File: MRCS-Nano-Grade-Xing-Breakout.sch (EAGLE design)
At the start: 24 parts, among them M2 SMALL_SERVO

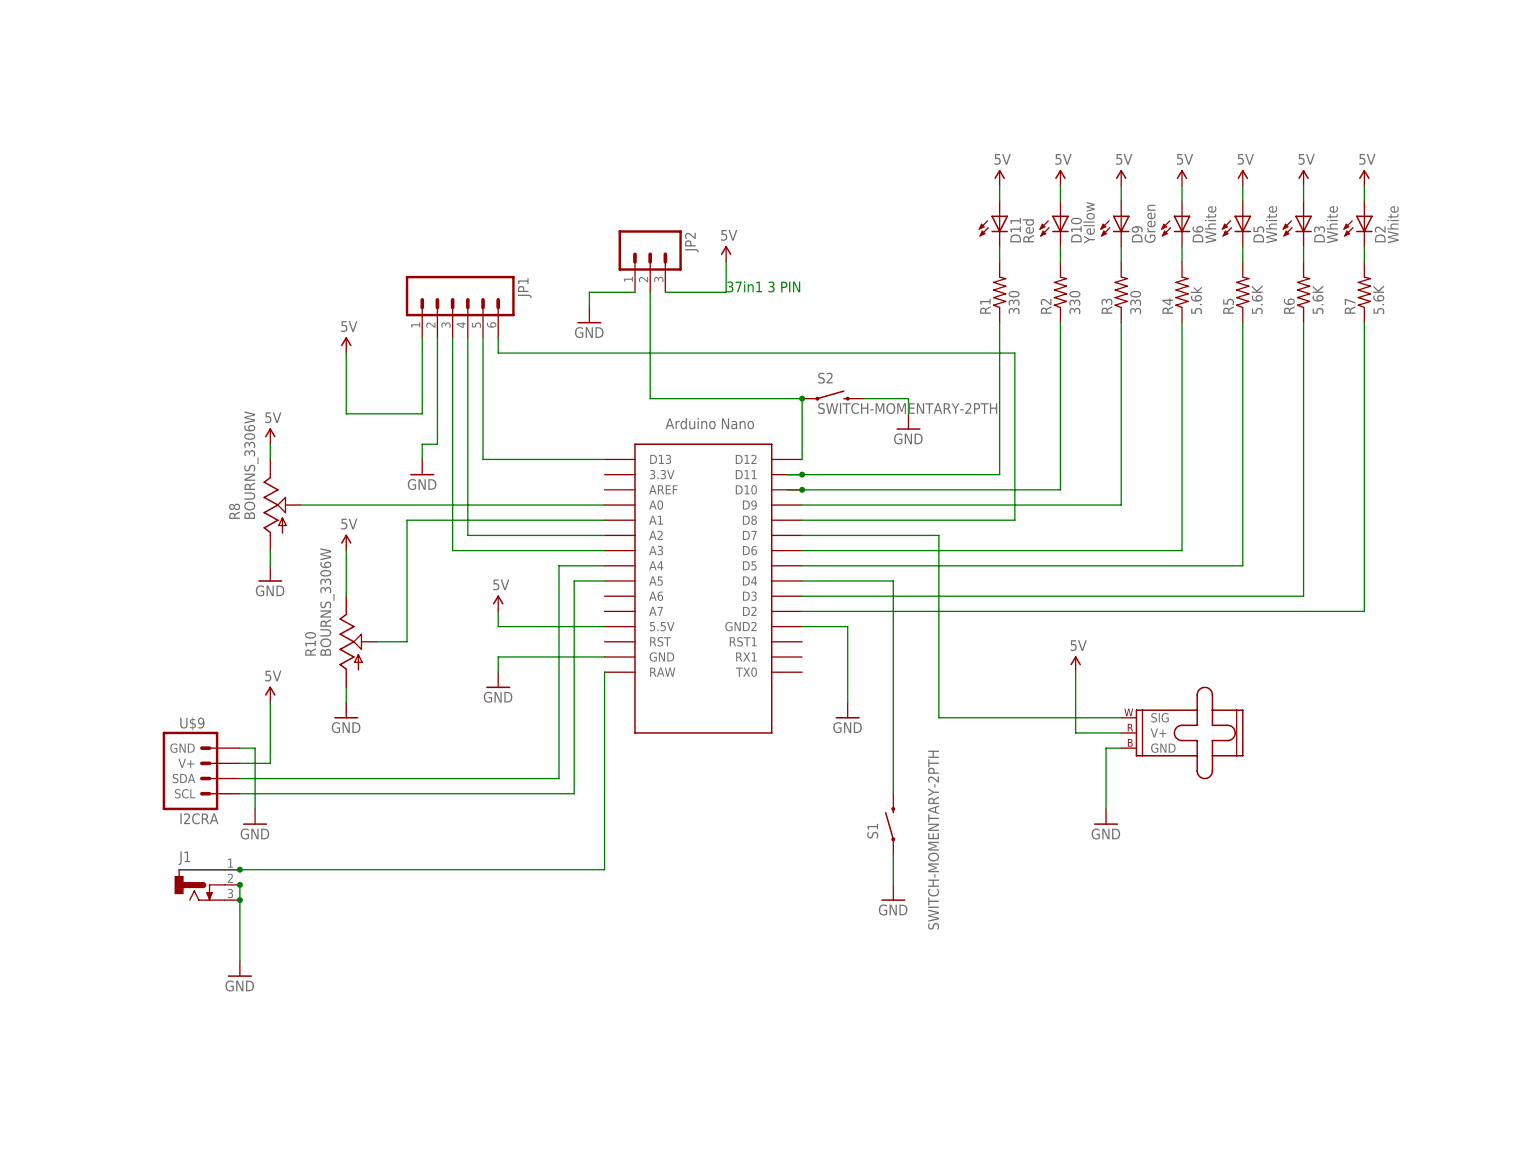
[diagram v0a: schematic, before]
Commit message: completed initial deisgn
After some consultation with Jon Schmidt this is ready to try for fab
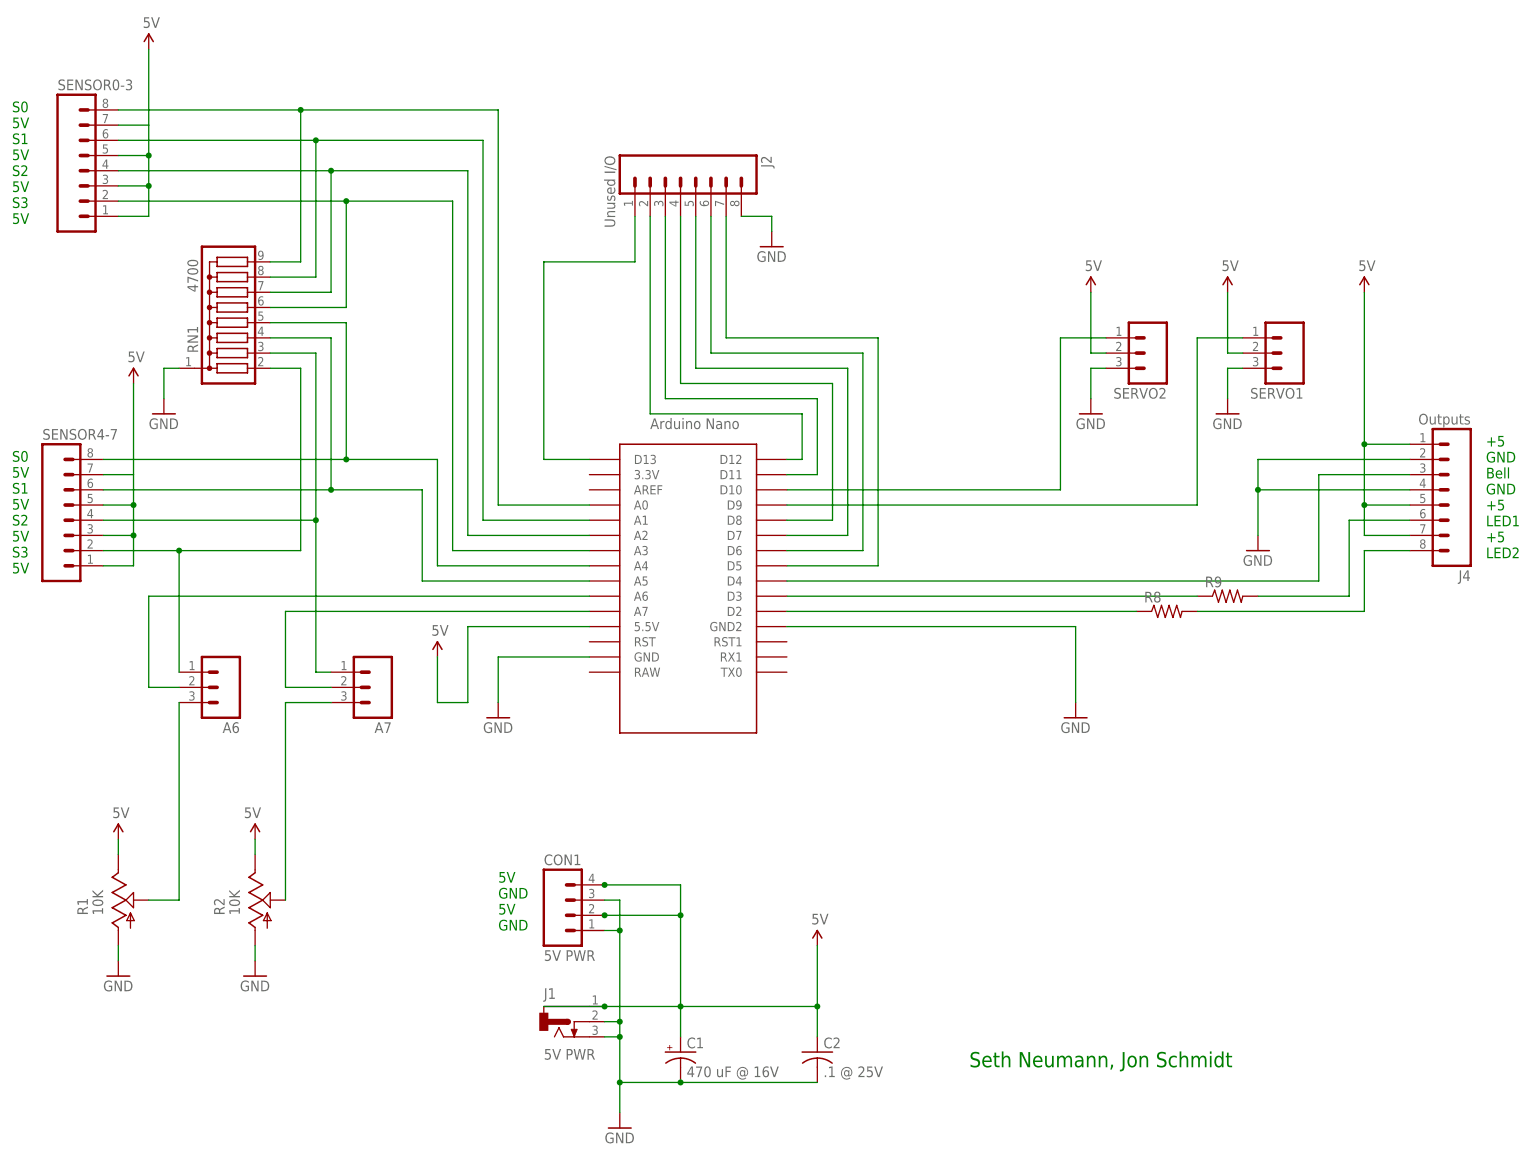
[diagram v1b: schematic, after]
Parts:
- removed D10: Yellow, SPCoast:LEDLED3MM
- removed D11: Red, SPCoast:LEDLED3MM
- removed D2, D3, D5, D6: White, SPCoast:LEDLED3MM
- removed D9: Green, SPCoast:LEDLED3MM
- removed JP1: (no value), SparkFun-Connectors:M06LOCK
- removed JP2: (no value), SparkFun-Connectors:M03LOCK
- removed M2: SMALL_SERVO, SparkFun-Electromechanical:SMALL_SERVO
- removed R10: BOURNS_3306W, mschutzer:BOURNS_3306W
- removed R3: 330, SparkFun-Resistors:RESISTORPTH-1/4W
- removed R4: 5.6k, SparkFun-Resistors:RESISTORPTH-1/4W
- removed R5, R6, R7: 5.6K, SparkFun-Resistors:RESISTORPTH-1/4W
- removed S1, S2: SWITCH-MOMENTARY-2PTH, SparkFun-Electromechanical:SWITCH-MOMENTARY-2PTH
- removed U$9: I2CRA, SPCoast-minimal:I2CRA
- added A6, A7, SERVO1, SERVO2: (no value), SparkFun-Connectors:M03LOCK
- added C1: 470 uF @ 16V, SPCoast:CAP-POLPTH-3.5MM
- added C2: .1 @ 25V, SPCoast:CAPPTH2
- added CON1: 5V PWR, SPCoast:CONNECTOR-M04SCREW_LOCK
- added J2: Unused I/O, SPCoast:CONNECTOR-M08LOCK
- added J4: Outputs, SPCoast:CONNECTOR-M08LOCK
- added R9: (no value), SPCoast:RPTH-R0
- added RN1: 4700, resistor-sil:G08R
- added SENSOR0-3, SENSOR4-7: (no value), SPCoast:CONNECTOR-M08LOCK
- J1: value (none) -> 5V PWR
- R1, R2: value 330 -> 10K; device SparkFun-Resistors:RESISTORPTH-1/4W -> pot:TRIM_US-RS3
- R8: value BOURNS_3306W -> (none); device mschutzer:BOURNS_3306W -> SPCoast:RPTH-R0
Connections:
- removed net A1: R10.S, U$1.A1
- removed net D10: R2.1, U$1.D10
- removed net D11: R1.1, U$1.D11
- removed net D12: JP2.2, S2.1, U$1.D12
- removed net D2: R7.1, U$1.D2
- removed net D3: R6.1, U$1.D3
- removed net D5: R5.1, U$1.D5
- removed net D6: R4.1, U$1.D6
- removed net D7: M2.SIG, U$1.D7
- removed net D9: R3.1, U$1.D9
- removed net SCL: U$1.A5, U$9.SCL
- removed net SDA: U$1.A4, U$9.SDA
- new net N$14: A6.3, R1.S
- new net N$15: A6.2, U$1.A6
- new net N$16: A7.2, U$1.A7
- new net N$17: RN1.8, SENSOR0-3.6, U$1.A1
- new net N$18: A7.3, R2.S
- new net N$19: J2.1, U$1.D13
- new net N$20: J2.2, U$1.D12
- new net N$21: J2.3, U$1.D11
- new net N$22: J2.4, U$1.D8
- new net N$23: J2.5, U$1.D7
- new net N$24: J2.6, U$1.D6
- new net N$25: J2.7, U$1.D5
- net 5V: now also C1.+, C2.1, CON1.2, CON1.4, J1.1, J4.1, J4.5, J4.7, R1.E, R2.E, SENSOR0-3.1, SENSOR0-3.3, SENSOR0-3.5, SENSOR0-3.7, SENSOR4-7.1, SENSOR4-7.3, SENSOR4-7.5, SENSOR4-7.7, SERVO1.2, SERVO2.2; no longer D10.A, D11.A, D2.A, D3.A, D5.A, D6.A, D9.A, JP1.1, JP2.3, M2.V+, R10.E, R8.E, U$9.V+
- net A0: now also RN1.9, SENSOR0-3.8; no longer R8.S
- net GND: now also C1.-, C2.2, CON1.1, CON1.3, J2.8, J4.2, J4.4, R1.A, R2.A, RN1.1, SERVO1.3, SERVO2.3; no longer JP1.2, JP2.1, M2.GND, R10.A, R8.A, S1.1, S2.2, U$9.GND
- net N$1: now also RN1.5, SENSOR4-7.8, U$1.A4; no longer J1.1, U$1.RAW
- net N$10: now also RN1.7, SENSOR0-3.4, U$1.A2; no longer JP1.5, U$1.D13
- net N$11: now also A7.1, RN1.3, SENSOR4-7.4; no longer JP1.6, U$1.D8
- net N$12: now also RN1.6, SENSOR0-3.2, U$1.A3; no longer JP1.4, U$1.A2
- net N$13: now also A6.1, RN1.2, SENSOR4-7.2; no longer JP1.3, U$1.A3
- net N$2: now also R8.1, U$1.D2; no longer D11.C, R1.2
- net N$3: now also J4.8, R8.2; no longer D10.C, R2.2
- net N$4: now also R9.1, U$1.D3; no longer D9.C, R3.2
- net N$5: now also J4.6, R9.2; no longer D6.C, R4.2
- net N$6: now also J4.3, U$1.D4; no longer D5.C, R5.2
- net N$7: now also RN1.4, SENSOR4-7.6, U$1.A5; no longer D3.C, R6.2
- net N$8: now also SERVO2.1, U$1.D10; no longer D2.C, R7.2
- net N$9: now also SERVO1.1, U$1.D9; no longer S1.2, U$1.D4
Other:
- note added: "+5 GND Bell GND +5 LED1 +5 LED2"
- note added: "5V GND 5V GND"
- note added: "S0 5V S1 5V S2 5V S3 5V"
- note added: "Seth Neumann, Jon Schmidt"
- note removed: "37in1 3 PIN"
- moved on the sheet: J1
